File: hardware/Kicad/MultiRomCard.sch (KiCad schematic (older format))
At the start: 17 parts, among them P1 VC4000_Cartridge_Bus, P2 MicroSD_Breakout, U1 Arduino_UNO, U2 74HC595, U3 74HC595, U4 74HC595, U5 6264, U6 74HC245, U7 74HC245, U8 74HC245

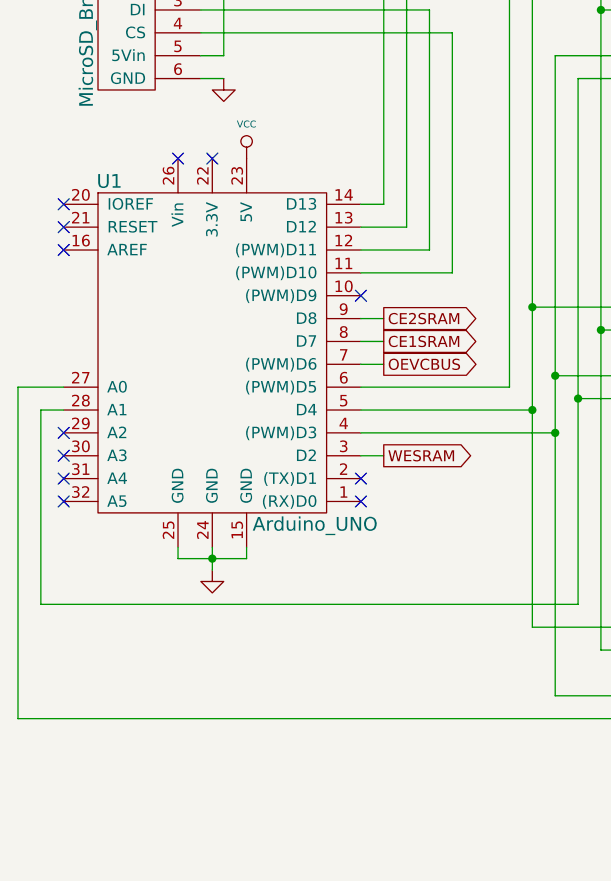
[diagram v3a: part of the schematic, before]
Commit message: [SCH/PCB] Replace Arduino UNO by Arduino Nano
- TODO: Shrink board outlines to account for smaller Arduino board.
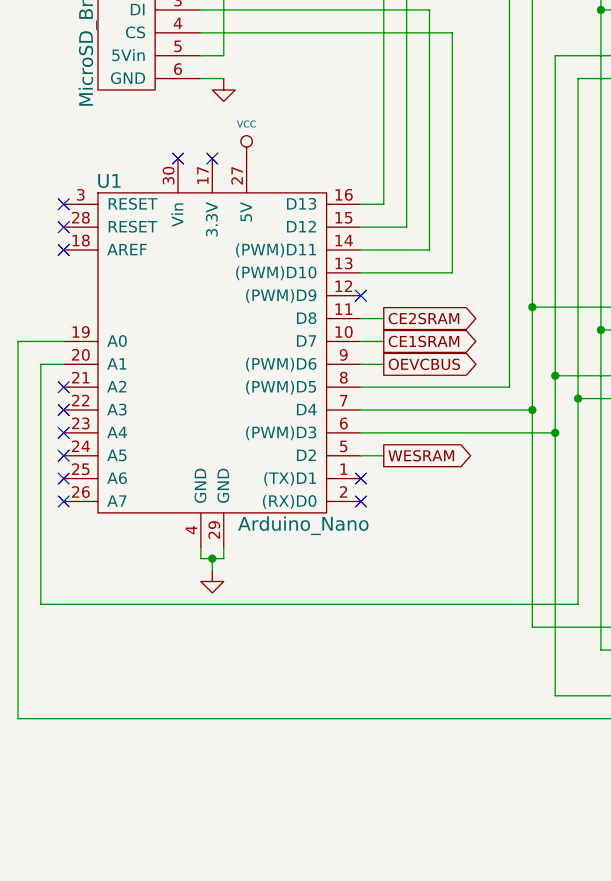
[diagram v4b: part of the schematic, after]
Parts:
- removed U1: Arduino_UNO, VC4000_MultiRom:Arduino_UNO, symbol Arduino_UNO
- added U1: Arduino_Nano, VC4000_MultiRom:Arduino_Nano, symbol Arduino_Nano
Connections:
- net CE1SRAM: now also U1.10 (D7)
- net CE2SRAM: now also U1.11 (D8)
- net GND: now also U1.29 (GND), U1.4 (GND)
- net OEVCBUS: now also U1.9 ((PWM)D6)
- net VCC: now also U1.27 (5V)
- net WESRAM: now also U1.5 (D2)
- net at U2.11 (SRCLK), U3.11 (SRCLK), U4.11 (SRCLK): now also U1.7 (D4)
- net at U2.12 (RCLK), U3.12 (RCLK), U4.12 (RCLK): now also U1.6 ((PWM)D3)
- net at U2.13 (G), U3.13 (G): now also U1.20 (A1)
- net at U2.14 (SER): now also U1.8 ((PWM)D5)
- net at U4.13 (G): now also U1.19 (A0)
- net at P2.4 (CS): now also U1.13 ((PWM)D10)
- net at P2.3 (DI): now also U1.14 ((PWM)D11)
- net at P2.2 (DO): now also U1.15 (D12)
- net at P2.1 (CLK): now also U1.16 (D13)
- no-connect marks 21 -> 23
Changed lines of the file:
@@
 NoConn ~ 10550 2350
 $Comp
-L VCC #PWR01
+L VCC #PWR13
 U 1 1 54D6D558
 P 10450 1600
-F 0 "#PWR01" H 10450 1700 30  0001 C CNN
+F 0 "#PWR13" H 10450 1700 30  0001 C CNN
 F 1 "VCC" H 10450 1750 30  0000 C CNN
 F 2 "" H 10450 1600 60  0000 C CNN
 F 3 "" H 10450 1600 60  0000 C CNN
 	1    10450 1600
-	1    0    0    -1
-$EndComp
-$Comp
-L Arduino_UNO U1
-U 1 1 54D6E609
-P 1550 3650
-F 0 "U1" H 1100 4400 60  0000 C CNN
-F 1 "Arduino_UNO" H 2000 2900 60  0000 C CNN
-F 2 "VC4000_MultiRom:Arduino_UNO" H 1550 3500 60  0001 C CNN
-F 3 "" H 1550 3500 60  0000 C CNN
-	1    1550 3650
 	1    0    0    -1
 $EndComp
@@
 NoConn ~ 900  3200
 $Comp
-L VCC #PWR02
+L VCC #PWR4
 U 1 1 54D739B7
 P 1700 2800
-F 0 "#PWR02" H 1700 2900 30  0001 C CNN
+F 0 "#PWR4" H 1700 2900 30  0001 C CNN
 F 1 "VCC" H 1700 2950 30  0000 C CNN
 F 2 "" H 1700 2800 60  0000 C CNN
@@
 NoConn ~ 2200 4200
 $Comp
-L VCC #PWR03
+L VCC #PWR5
 U 1 1 54DB48BB
 P 3250 1650
-F 0 "#PWR03" H 3250 1750 30  0001 C CNN
+F 0 "#PWR5" H 3250 1750 30  0001 C CNN
 F 1 "VCC" H 3250 1800 30  0000 C CNN
 F 2 "" H 3250 1650 60  0000 C CNN
@@
 $EndComp
 $Comp
-L GND #PWR04
+L GND #PWR9
 U 1 1 54DB55F6
 P 9500 3050
-F 0 "#PWR04" H 9500 3050 30  0001 C CNN
+F 0 "#PWR9" H 9500 3050 30  0001 C CNN
 F 1 "GND" H 9500 2980 30  0001 C CNN
 F 2 "" H 9500 3050 60  0000 C CNN
@@
 $EndComp
 $Comp
-L VCC #PWR05
+L VCC #PWR11
 U 1 1 54DB5800
 P 9550 4300
-F 0 "#PWR05" H 9550 4400 30  0001 C CNN
+F 0 "#PWR11" H 9550 4400 30  0001 C CNN
 F 1 "VCC" H 9550 4450 30  0000 C CNN
 F 2 "" H 9550 4300 60  0000 C CNN
@@
 NoConn ~ 9450 3950
 $Comp
-L GND #PWR06
+L GND #PWR14
 U 1 1 54DB7B7A
 P 10450 4900
-F 0 "#PWR06" H 10450 4900 30  0001 C CNN
+F 0 "#PWR14" H 10450 4900 30  0001 C CNN
 F 1 "GND" H 10450 4830 30  0001 C CNN
 F 2 "" H 10450 4900 60  0000 C CNN
@@
 $EndComp
 $Comp
-L GND #PWR07
+L GND #PWR10
 U 1 1 54DB8BDD
 P 9550 3900
-F 0 "#PWR07" H 9550 3900 30  0001 C CNN
+F 0 "#PWR10" H 9550 3900 30  0001 C CNN
 F 1 "GND" H 9550 3830 30  0001 C CNN
 F 2 "" H 9550 3900 60  0000 C CNN
@@
 NoConn ~ 900  4200
 NoConn ~ 900  4300
-$Comp
-L GND #PWR08
-U 1 1 54D739DD
-P 1550 4600
-F 0 "#PWR08" H 1550 4600 30  0001 C CNN
-F 1 "GND" H 1550 4530 30  0001 C CNN
-F 2 "" H 1550 4600 60  0000 C CNN
-F 3 "" H 1550 4600 60  0000 C CNN
-	1    1550 4600
-	1    0    0    -1
-$EndComp
 Text Notes 10200 3750 0    60   ~ 0
 "CE2"
@@
 $EndComp
 $Comp
-L GND #PWR09
+L GND #PWR7
 U 1 1 558564D3
 P 8100 6200
-F 0 "#PWR09" H 8100 6200 30  0001 C CNN
+F 0 "#PWR7" H 8100 6200 30  0001 C CNN
 F 1 "GND" H 8100 6130 30  0001 C CNN
 F 2 "" H 8100 6200 60  0000 C CNN
@@
 $EndComp
 $Comp
-L VCC #PWR010
+L VCC #PWR6
 U 1 1 5585650E
 P 8100 5900
-F 0 "#PWR010" H 8100 6000 30  0001 C CNN
+F 0 "#PWR6" H 8100 6000 30  0001 C CNN
 F 1 "VCC" H 8100 6050 30  0000 C CNN
 F 2 "" H 8100 5900 60  0000 C CNN
@@
 IC Power Decoupling Caps
 $Comp
-L GND #PWR011
+L GND #PWR8
 U 1 1 5587E073
 P 9450 1500
-F 0 "#PWR011" H 9450 1500 30  0001 C CNN
+F 0 "#PWR8" H 9450 1500 30  0001 C CNN
 F 1 "GND" H 9450 1430 30  0001 C CNN
 F 2 "" H 9450 1500 60  0000 C CNN
@@
 $EndComp
 $Comp
-L GND #PWR012
+L GND #PWR12
 U 1 1 5587E24F
 P 10350 2050
-F 0 "#PWR012" H 10350 2050 30  0001 C CNN
+F 0 "#PWR12" H 10350 2050 30  0001 C CNN
 F 1 "GND" H 10350 1980 30  0001 C CNN
 F 2 "" H 10350 2050 60  0000 C CNN
@@
 $EndComp
 $Comp
-L GND #PWR013
+L GND #PWR3
 U 1 1 5587EA58
 P 1600 2450
-F 0 "#PWR013" H 1600 2450 30  0001 C CNN
+F 0 "#PWR3" H 1600 2450 30  0001 C CNN
 F 1 "GND" H 1600 2380 30  0001 C CNN
 F 2 "" H 1600 2450 60  0000 C CNN
@@
 	2850 1850 3450 1850
 Wire Wire Line
-	900  3800 700  3800
-Wire Wire Line
-	700  3800 700  5250
+	700  3600 700  5250
 Wire Wire Line
 	700  5250 3450 5250
-Wire Wire Line
-	800  3900 900  3900
 Wire Wire Line
 	3150 4750 800  4750
@@
 Connection ~ 3150 3850
 Wire Wire Line
-	800  4750 800  3900
+	800  4750 800  3700
 Wire Wire Line
 	2950 3900 2200 3900
@@
 Connection ~ 8300 6200
 Wire Wire Line
-	1400 4500 1400 4550
-Wire Wire Line
-	1400 4550 1700 4550
-Wire Wire Line
-	1550 4500 1550 4600
-Wire Wire Line
-	1700 4550 1700 4500
-Connection ~ 1550 4550
-Wire Wire Line
 	1500 2350 1600 2350
 Wire Wire Line
@@
 	1500 2450 1600 2450
 $Comp
-L VCC #PWR014
+L VCC #PWR2
 U 1 1 5587FD9D
 P 1600 1650
-F 0 "#PWR014" H 1600 1750 30  0001 C CNN
+F 0 "#PWR2" H 1600 1750 30  0001 C CNN
 F 1 "VCC" H 1600 1800 30  0000 C CNN
 F 2 "" H 1600 1650 60  0000 C CNN
@@
 	-1   0    0    -1
 $EndComp
+$Comp
+L Arduino_Nano U1
+U 1 1 558812C5
+P 1550 3650
+F 0 "U1" H 1100 4400 60  0000 C CNN
+F 1 "Arduino_Nano" H 1950 2900 60  0000 C CNN
+F 2 "VC4000_MultiRom:Arduino_Nano" H 1550 3500 60  0001 C CNN
+F 3 "" H 1550 3500 60  0000 C CNN
+	1    1550 3650
+	1    0    0    -1
+$EndComp
+Wire Wire Line
+	800  3700 900  3700
+Wire Wire Line
+	700  3600 900  3600
+NoConn ~ 900  3800
+NoConn ~ 900  3900
+$Comp
+L GND #PWR1
+U 1 1 54D739DD
+P 1550 4600
+F 0 "#PWR1" H 1550 4600 30  0001 C CNN
+F 1 "GND" H 1550 4530 30  0001 C CNN
+F 2 "" H 1550 4600 60  0000 C CNN
+F 3 "" H 1550 4600 60  0000 C CNN
+	1    1550 4600
+	1    0    0    -1
+$EndComp
+Wire Wire Line
+	1500 4500 1500 4550
+Wire Wire Line
+	1500 4550 1600 4550
+Wire Wire Line
+	1600 4550 1600 4500
+Wire Wire Line
+	1550 4550 1550 4600
+Connection ~ 1550 4550
 $EndSCHEMATC

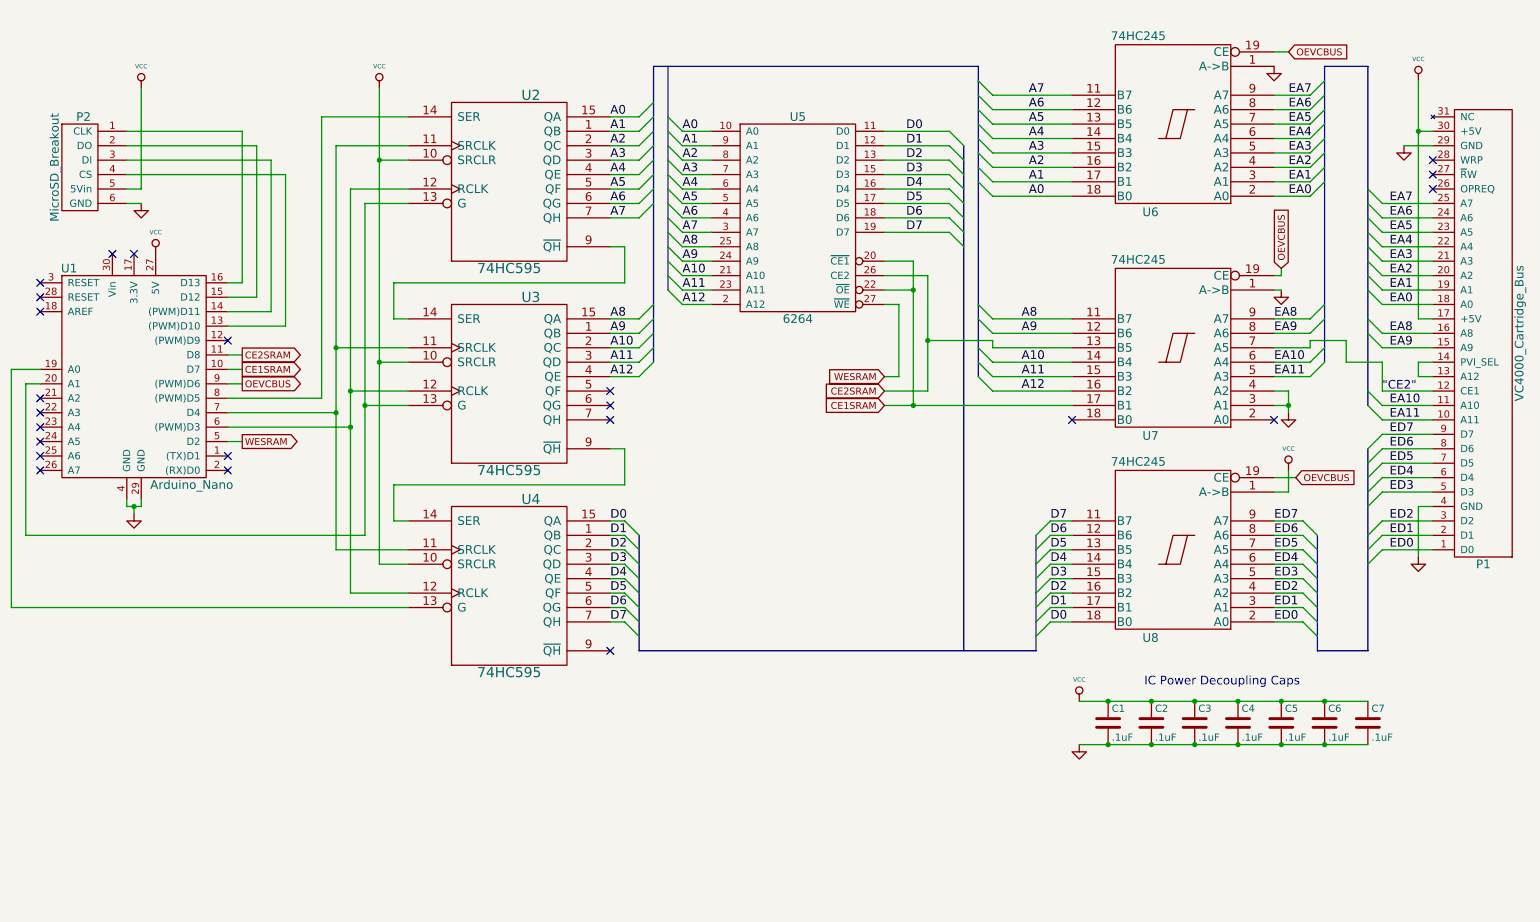
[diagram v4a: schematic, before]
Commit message: [SCH/PCB] Add pin header for testing purposes.
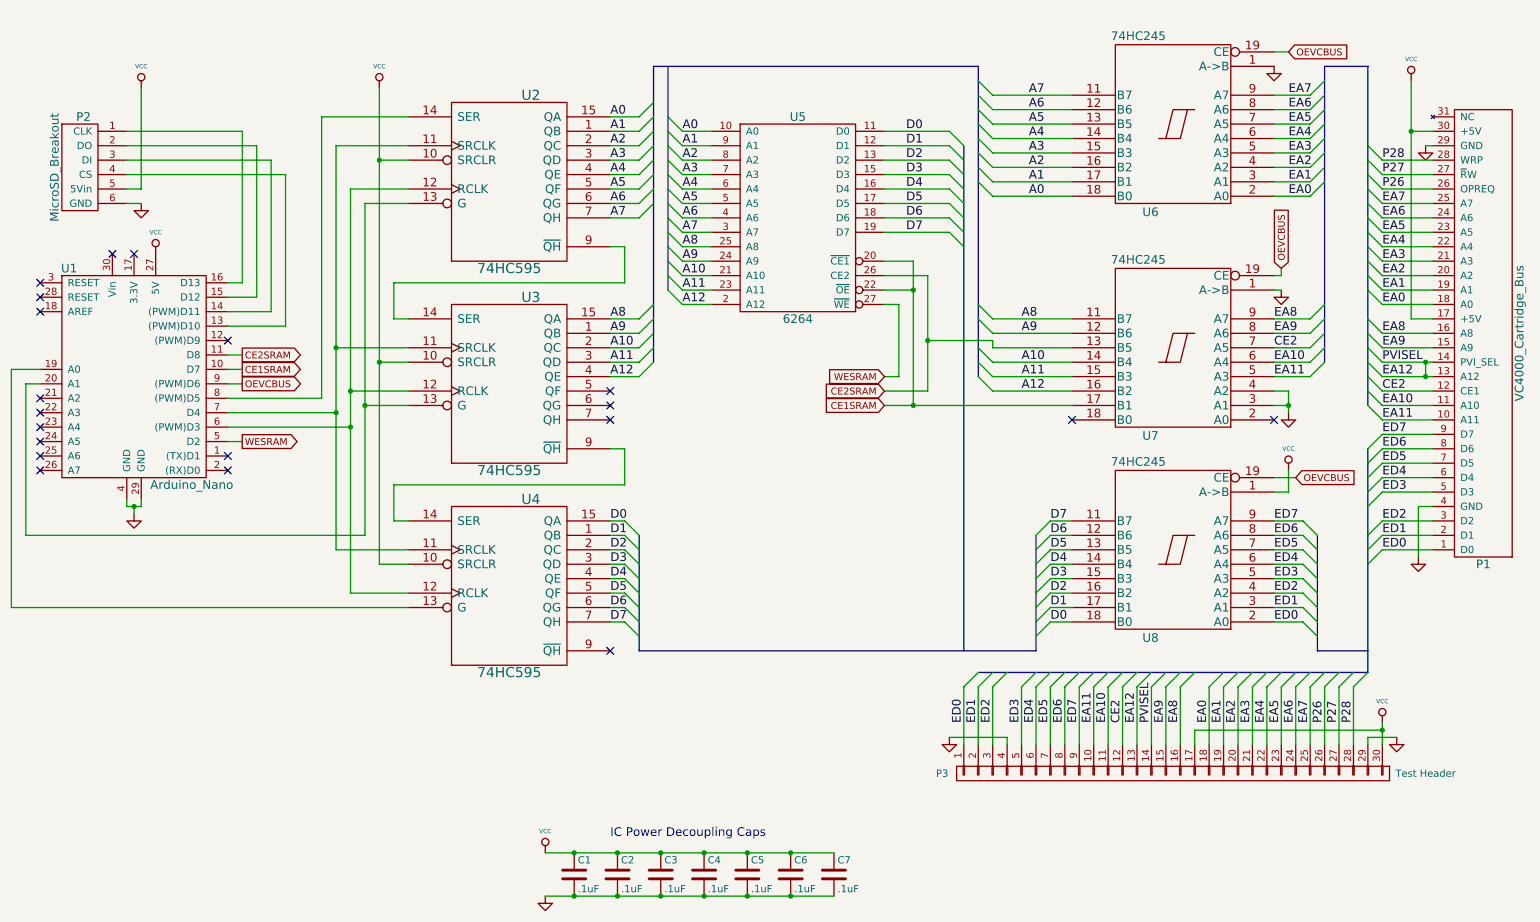
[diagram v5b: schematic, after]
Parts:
- added P3: Test Header, Pin_Headers:Pin_Header_Straight_1x30, symbol CONN_01X30
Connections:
- net EA0: now also P3.18 (P18)
- net EA1: now also P3.19 (P19)
- net EA10: now also P3.11 (P11)
- net EA11: now also P3.10 (P10)
- net EA2: now also P3.20 (P20)
- net EA3: now also P3.21 (P21)
- net EA4: now also P3.22 (P22)
- net EA5: now also P3.23 (P23)
- net EA6: now also P3.24 (P24)
- net EA7: now also P3.25 (P25)
- net EA8: now also P3.16 (P16)
- net EA9: now also P3.15 (P15)
- net ED0: now also P3.1 (P1)
- net ED1: now also P3.2 (P2)
- net ED2: now also P3.3 (P3)
- net ED3: now also P3.5 (P5)
- net ED4: now also P3.6 (P6)
- net ED5: now also P3.7 (P7)
- net ED6: now also P3.8 (P8)
- net ED7: now also P3.9 (P9)
- net GND: now also P3.29 (P29), P3.4 (P4)
- net VCC: now also P3.17 (P17), P3.30 (P30)
- net CE2: now reaches P1.12 (CE1), U7.7 (A5)
- net CE2: now also P3.12 (P12)
- net EA12: now reaches P1.13 (A12), P1.14 (PVI_SEL)
- net EA12: now also P3.13 (P13), P3.14 (P14)
- net P26: now reaches P1.26 (OPREQ)
- net P26: now also P3.26 (P26)
- net P27: now reaches P1.27 (~R~W)
- net P27: now also P3.27 (P27)
- net P28: now reaches P1.28 (WRP)
- net P28: now also P3.28 (P28)
- no-connect marks 23 -> 20
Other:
- note removed: ""CE2""
- moved on the sheet: C1, C2, C3, C4, C5, C6, C7
